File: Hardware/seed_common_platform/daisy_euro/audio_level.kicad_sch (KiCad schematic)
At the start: 28 parts, among them U4 TL074CPWR, U5 TL074CPWR

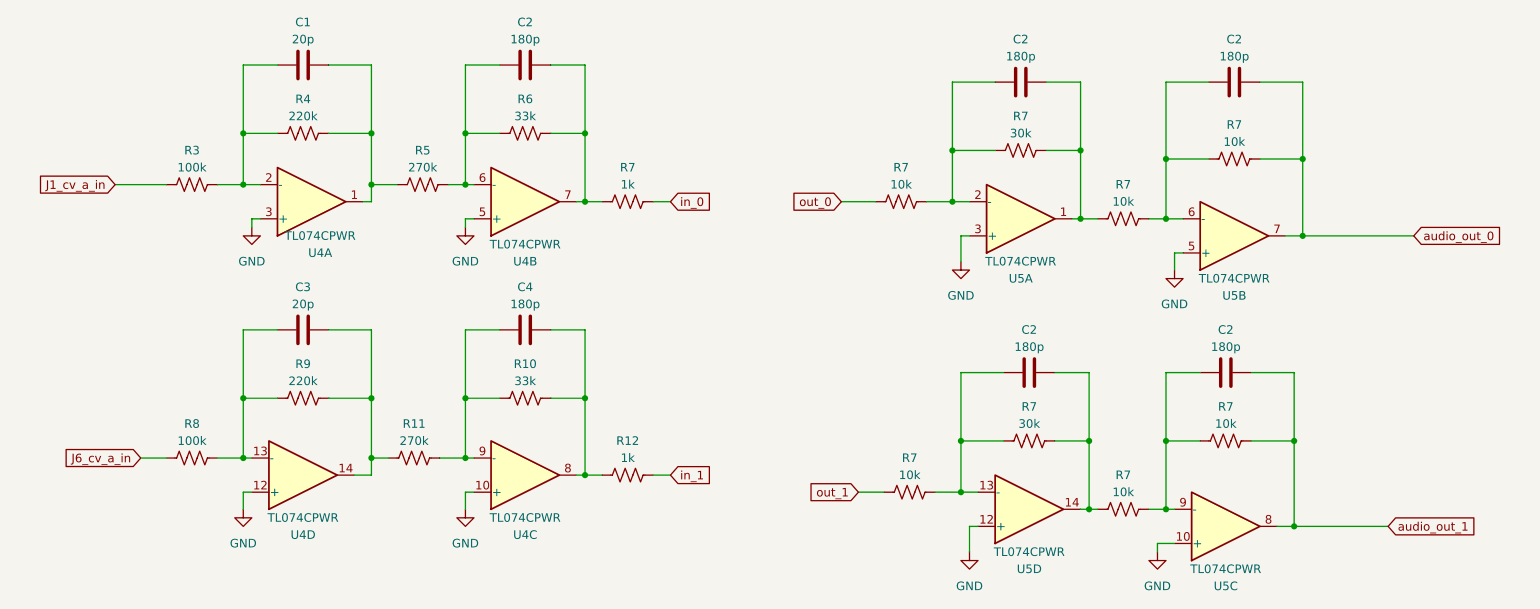
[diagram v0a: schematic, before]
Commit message: fix rev A errors
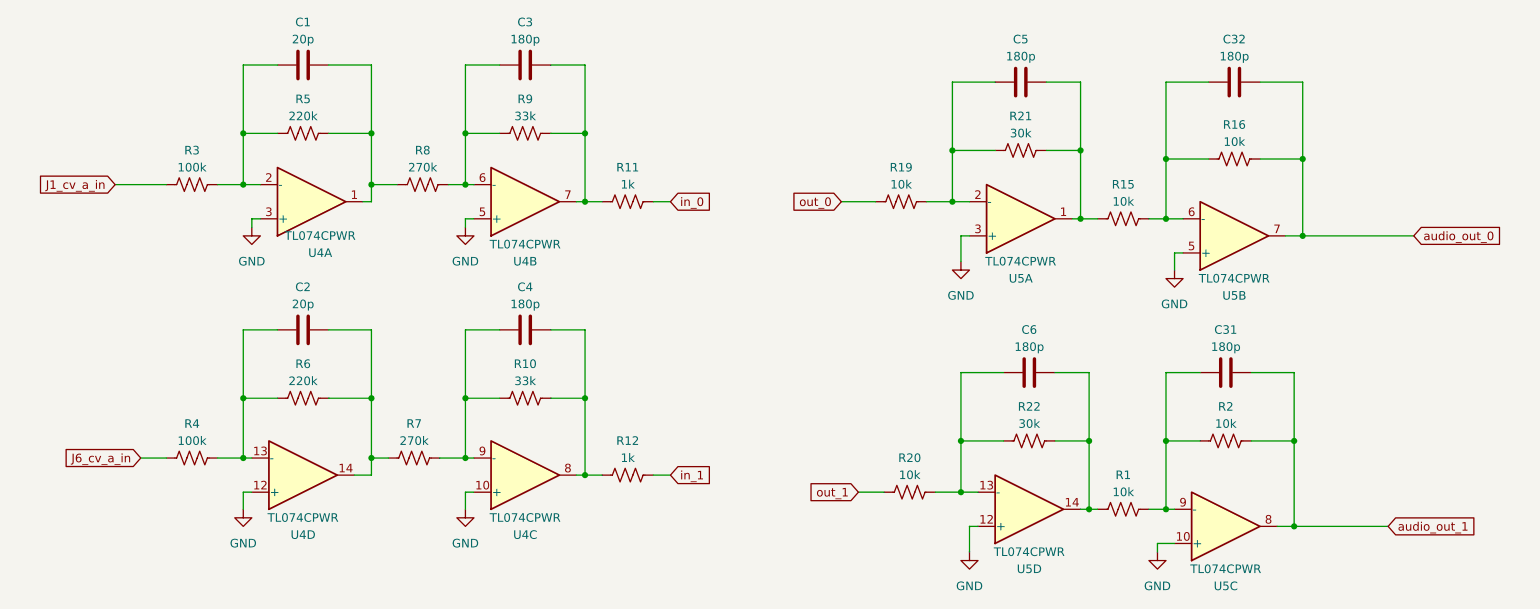
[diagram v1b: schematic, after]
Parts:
- renumbered C3 to C2, C2 to C3, C2 to C31, C2 to C32, C2 to C5, C2 to C6, R7 to R1, R7 to R11, R7 to R15, R7 to R16, R7 to R19, R7 to R2, R7 to R20, R7 to R21, R7 to R22, R8 to R4, R4 to R5, R9 to R6, R11 to R7, R5 to R8, R6 to R9
